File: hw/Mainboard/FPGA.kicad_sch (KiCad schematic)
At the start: 62 parts, among them J5 PMOD1, J6 PMOD2, J7 PROG, J8 FPGA_MCU, J9 BUS_EXPANSION, Q1 MMBT3904, SW3 CONFIG, U10 T8Q144C3

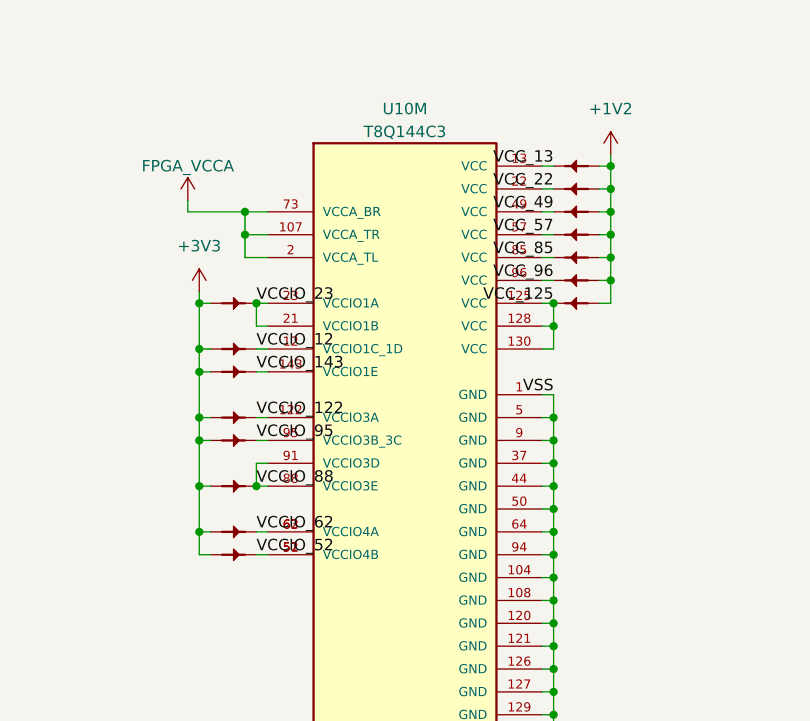
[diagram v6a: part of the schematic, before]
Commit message: hw: touchups to FPGA power (wip)
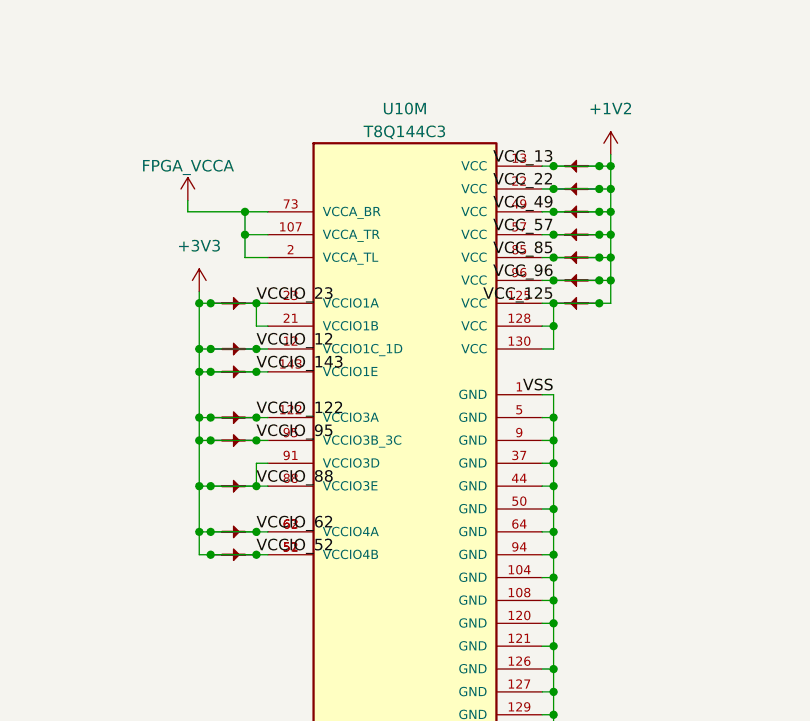
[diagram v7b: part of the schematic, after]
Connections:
- net VCCIO_12 is gone; now on net +3V3: PT23.2, U10.12 (VCCIO1C_1D)
- net VCCIO_122 is gone; now on net +3V3: PT25.2, U10.122 (VCCIO3A)
- net VCCIO_143 is gone; now on net +3V3: PT24.2, U10.143 (VCCIO1E)
- net VCCIO_23 is gone; now on net +3V3: PT21.2, U10.21 (VCCIO1B), U10.23 (VCCIO1A)
- net VCCIO_52 is gone; now on net +3V3: PT29.2, U10.51 (VCCIO4B), U10.52 (VCCIO4B)
- net VCCIO_62 is gone; now on net +3V3: PT28.2, U10.62 (VCCIO4A), U10.63 (VCCIO4A)
- net VCCIO_88 is gone; now on net +3V3: PT27.2, U10.88 (VCCIO3E), U10.91 (VCCIO3D)
- net VCCIO_95 is gone; now on net +3V3: PT26.2, U10.95 (VCCIO3B_3C)
- net VCC_125 is gone; now on net +1V2: PT22.2, U10.125 (VCC), U10.128 (VCC), U10.130 (VCC)
- net VCC_13 is gone; now on net +1V2: PT15.2, U10.13 (VCC)
- net VCC_22 is gone; now on net +1V2: PT16.2, U10.22 (VCC)
- net VCC_49 is gone; now on net +1V2: PT17.2, U10.49 (VCC)
- net VCC_57 is gone; now on net +1V2: PT18.2, U10.57 (VCC)
- net VCC_85 is gone; now on net +1V2: PT19.2, U10.85 (VCC)
- net VCC_96 is gone; now on net +1V2: PT20.2, U10.96 (VCC)
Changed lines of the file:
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@@
   (junction (at 82.55 233.68) (diameter 0) (color 0 0 0 0)
   )
+  (junction (at 100.33 152.4) (diameter 0) (color 0 0 0 0)
+  )
   (junction (at 400.05 153.67) (diameter 0) (color 0 0 0 0)
   )
@@
   (junction (at 125.73 259.08) (diameter 0) (color 0 0 0 0)
   )
+  (junction (at 100.33 157.48) (diameter 0) (color 0 0 0 0)
+  )
   (junction (at 95.25 187.96) (diameter 0) (color 0 0 0 0)
   )
@@
   (junction (at 95.25 205.74) (diameter 0) (color 0 0 0 0)
   )
+  (junction (at 57.15 187.96) (diameter 0) (color 0 0 0 0)
+  )
   (junction (at 19.05 64.77) (diameter 0) (color 0 0 0 0)
   )
@@
   (junction (at 36.83 259.08) (diameter 0) (color 0 0 0 0)
   )
+  (junction (at 57.15 165.1) (diameter 0) (color 0 0 0 0)
+  )
+  (junction (at 62.23 187.96) (diameter 0) (color 0 0 0 0)
+  )
   (junction (at 55.88 29.21) (diameter 0) (color 0 0 0 0)
   )
@@
   (junction (at 44.45 241.3) (diameter 0) (color 0 0 0 0)
   )
+  (junction (at 62.23 165.1) (diameter 0) (color 0 0 0 0)
+  )
   (junction (at 19.05 241.3) (diameter 0) (color 0 0 0 0)
   )
+  (junction (at 95.25 152.4) (diameter 0) (color 0 0 0 0)
+  )
   (junction (at 364.49 161.29) (diameter 0) (color 0 0 0 0)
   )
@@
   (junction (at 57.15 233.68) (diameter 0) (color 0 0 0 0)
   )
+  (junction (at 57.15 167.64) (diameter 0) (color 0 0 0 0)
+  )
+  (junction (at 57.15 180.34) (diameter 0) (color 0 0 0 0)
+  )
   (junction (at 58.42 29.21) (diameter 0) (color 0 0 0 0)
   )
@@
   (junction (at 50.8 41.91) (diameter 0) (color 0 0 0 0)
   )
+  (junction (at 95.25 147.32) (diameter 0) (color 0 0 0 0)
+  )
   (junction (at 336.55 10.16) (diameter 0) (color 0 0 0 0)
   )
@@
   (junction (at 95.25 190.5) (diameter 0) (color 0 0 0 0)
   )
+  (junction (at 62.23 175.26) (diameter 0) (color 0 0 0 0)
+  )
   (junction (at 49.53 259.08) (diameter 0) (color 0 0 0 0)
   )
   (junction (at 95.25 198.12) (diameter 0) (color 0 0 0 0)
   )
+  (junction (at 95.25 154.94) (diameter 0) (color 0 0 0 0)
+  )
   (junction (at 60.96 149.86) (diameter 0) (color 0 0 0 0)
   )
@@
   (junction (at 101.6 157.48) (diameter 0) (color 0 0 0 0)
   )
+  (junction (at 100.33 160.02) (diameter 0) (color 0 0 0 0)
+  )
   (junction (at 95.25 172.72) (diameter 0) (color 0 0 0 0)
   )
@@
   (junction (at 382.27 17.78) (diameter 0) (color 0 0 0 0)
   )
+  (junction (at 62.23 172.72) (diameter 0) (color 0 0 0 0)
+  )
   (junction (at 55.88 160.02) (diameter 0) (color 0 0 0 0)
   )
@@
   (junction (at 138.43 251.46) (diameter 0) (color 0 0 0 0)
   )
+  (junction (at 100.33 144.78) (diameter 0) (color 0 0 0 0)
+  )
   (junction (at 60.96 152.4) (diameter 0) (color 0 0 0 0)
   )
   (junction (at 53.34 29.21) (diameter 0) (color 0 0 0 0)
   )
+  (junction (at 62.23 185.42) (diameter 0) (color 0 0 0 0)
+  )
   (junction (at 69.85 233.68) (diameter 0) (color 0 0 0 0)
   )
@@
   (junction (at 15.24 57.15) (diameter 0) (color 0 0 0 0)
   )
+  (junction (at 57.15 185.42) (diameter 0) (color 0 0 0 0)
+  )
   (junction (at 107.95 241.3) (diameter 0) (color 0 0 0 0)
   )
@@
   (junction (at 55.88 185.42) (diameter 0) (color 0 0 0 0)
   )
+  (junction (at 100.33 154.94) (diameter 0) (color 0 0 0 0)
+  )
+  (junction (at 95.25 144.78) (diameter 0) (color 0 0 0 0)
+  )
   (junction (at 55.88 167.64) (diameter 0) (color 0 0 0 0)
   )
@@
   (junction (at 74.93 251.46) (diameter 0) (color 0 0 0 0)
   )
+  (junction (at 100.33 149.86) (diameter 0) (color 0 0 0 0)
+  )
   (junction (at 69.85 241.3) (diameter 0) (color 0 0 0 0)
   )
+  (junction (at 57.15 172.72) (diameter 0) (color 0 0 0 0)
+  )
   (junction (at 323.85 88.9) (diameter 0) (color 0 0 0 0)
   )
@@
   (junction (at 365.76 129.54) (diameter 0) (color 0 0 0 0)
   )
+  (junction (at 100.33 147.32) (diameter 0) (color 0 0 0 0)
+  )
+  (junction (at 57.15 175.26) (diameter 0) (color 0 0 0 0)
+  )
+  (junction (at 62.23 167.64) (diameter 0) (color 0 0 0 0)
+  )
   (junction (at 95.25 175.26) (diameter 0) (color 0 0 0 0)
   )
@@
   (junction (at 62.23 180.34) (diameter 0) (color 0 0 0 0)
   )
+  (junction (at 95.25 157.48) (diameter 0) (color 0 0 0 0)
+  )
   (junction (at 49.53 251.46) (diameter 0) (color 0 0 0 0)
   )
@@
   (junction (at 55.88 172.72) (diameter 0) (color 0 0 0 0)
   )
+  (junction (at 95.25 149.86) (diameter 0) (color 0 0 0 0)
+  )
   (junction (at 95.25 208.28) (diameter 0) (color 0 0 0 0)
   )
@@
   (junction (at 58.42 54.61) (diameter 0) (color 0 0 0 0)
   )
+  (junction (at 57.15 160.02) (diameter 0) (color 0 0 0 0)
+  )
   (junction (at 401.32 10.16) (diameter 0) (color 0 0 0 0)
   )
@@
     (stroke (width 0) (type default) (color 0 0 0 0))
   )
+  (wire (pts (xy 57.15 172.72) (xy 62.23 172.72))
+    (stroke (width 0) (type default) (color 0 0 0 0))
+  )
   (wire (pts (xy 53.34 44.45) (xy 67.31 44.45))
     (stroke (width 0) (type default) (color 0 0 0 0))
@@
     (stroke (width 0) (type default) (color 0 0 0 0))
   )
+  (wire (pts (xy 57.15 175.26) (xy 62.23 175.26))
+    (stroke (width 0) (type default) (color 0 0 0 0))
+  )
   (wire (pts (xy 55.88 180.34) (xy 55.88 185.42))
     (stroke (width 0) (type default) (color 0 0 0 0))
@@
     (stroke (width 0) (type default) (color 0 0 0 0))
   )
+  (wire (pts (xy 95.25 157.48) (xy 100.33 157.48))
+    (stroke (width 0) (type default) (color 0 0 0 0))
+  )
   (wire (pts (xy 382.27 153.67) (xy 400.05 153.67))
     (stroke (width 0) (type default) (color 0 0 0 0))
@@
     (stroke (width 0) (type default) (color 0 0 0 0))
   )
+  (wire (pts (xy 95.25 152.4) (xy 100.33 152.4))
+    (stroke (width 0) (type default) (color 0 0 0 0))
+  )
   (wire (pts (xy 368.3 106.68) (xy 377.19 106.68))
     (stroke (width 0) (type default) (color 0 0 0 0))
@@
     (stroke (width 0) (type default) (color 0 0 0 0))
   )
+  (wire (pts (xy 57.15 165.1) (xy 62.23 165.1))
+    (stroke (width 0) (type default) (color 0 0 0 0))
+  )
   (wire (pts (xy 62.23 257.81) (xy 62.23 259.08))
     (stroke (width 0) (type default) (color 0 0 0 0))
@@
     (stroke (width 0) (type default) (color 0 0 0 0))
   )
+  (wire (pts (xy 57.15 185.42) (xy 62.23 185.42))
+    (stroke (width 0) (type default) (color 0 0 0 0))
+  )
   (wire (pts (xy 364.49 161.29) (xy 364.49 167.64))
     (stroke (width 0) (type default) (color 0 0 0 0))
@@
     (stroke (width 0) (type default) (color 0 0 0 0))
   )
+  (wire (pts (xy 95.25 147.32) (xy 100.33 147.32))
+    (stroke (width 0) (type default) (color 0 0 0 0))
+  )
   (wire (pts (xy 54.61 149.86) (xy 54.61 148.59))
     (stroke (width 0) (type default) (color 0 0 0 0))
@@
     (stroke (width 0) (type default) (color 0 0 0 0))
   )
+  (wire (pts (xy 57.15 160.02) (xy 62.23 160.02))
+    (stroke (width 0) (type default) (color 0 0 0 0))
+  )
   (wire (pts (xy 336.55 10.16) (xy 336.55 11.43))
     (stroke (width 0) (type default) (color 0 0 0 0))
   )
+  (wire (pts (xy 95.25 160.02) (xy 100.33 160.02))
+    (stroke (width 0) (type default) (color 0 0 0 0))
+  )
   (wire (pts (xy 140.97 41.91) (xy 128.27 41.91))
     (stroke (width 0) (type default) (color 0 0 0 0))
@@
     (stroke (width 0) (type default) (color 0 0 0 0))
   )
+  (wire (pts (xy 95.25 154.94) (xy 100.33 154.94))
+    (stroke (width 0) (type default) (color 0 0 0 0))
+  )
   (wire (pts (xy 389.89 91.44) (xy 394.97 91.44))
     (stroke (width 0) (type default) (color 0 0 0 0))
@@
     (stroke (width 0) (type default) (color 0 0 0 0))
   )
+  (wire (pts (xy 95.25 144.78) (xy 100.33 144.78))
+    (stroke (width 0) (type default) (color 0 0 0 0))
+  )
   (wire (pts (xy 402.59 50.8) (xy 402.59 52.07))
     (stroke (width 0) (type default) (color 0 0 0 0))
@@
     (stroke (width 0) (type default) (color 0 0 0 0))
   )
+  (wire (pts (xy 57.15 167.64) (xy 62.23 167.64))
+    (stroke (width 0) (type default) (color 0 0 0 0))
+  )
   (wire (pts (xy 411.48 41.91) (xy 411.48 43.18))
     (stroke (width 0) (type default) (color 0 0 0 0))
@@
     (stroke (width 0) (type default) (color 0 0 0 0))
   )
+  (wire (pts (xy 57.15 187.96) (xy 62.23 187.96))
+    (stroke (width 0) (type default) (color 0 0 0 0))
+  )
   (wire (pts (xy 100.33 154.94) (xy 101.6 154.94))
     (stroke (width 0) (type default) (color 0 0 0 0))
@@
     (stroke (width 0) (type default) (color 0 0 0 0))
   )
+  (wire (pts (xy 57.15 180.34) (xy 62.23 180.34))
+    (stroke (width 0) (type default) (color 0 0 0 0))
+  )
   (wire (pts (xy 95.25 198.12) (xy 95.25 200.66))
     (stroke (width 0) (type default) (color 0 0 0 0))
@@
     (stroke (width 0) (type default) (color 0 0 0 0))
   )
+  (wire (pts (xy 95.25 149.86) (xy 100.33 149.86))
+    (stroke (width 0) (type default) (color 0 0 0 0))
+  )

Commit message: hw: caps & logos (wip)
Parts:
- removed C92: 10u, Capacitor_SMD:C_0603_1608Metric, symbol Device:C_Small
- added C99: 1u, Capacitor_SMD:C_0402_1005Metric, symbol Device:C_Small
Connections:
- net +3V3: now also C99.1
- net PD_GND: now also C99.2
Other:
- title: CBM PET Mainboard Replacement -> EconoPET 40/8096
